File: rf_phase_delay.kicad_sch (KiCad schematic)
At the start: 0 parts

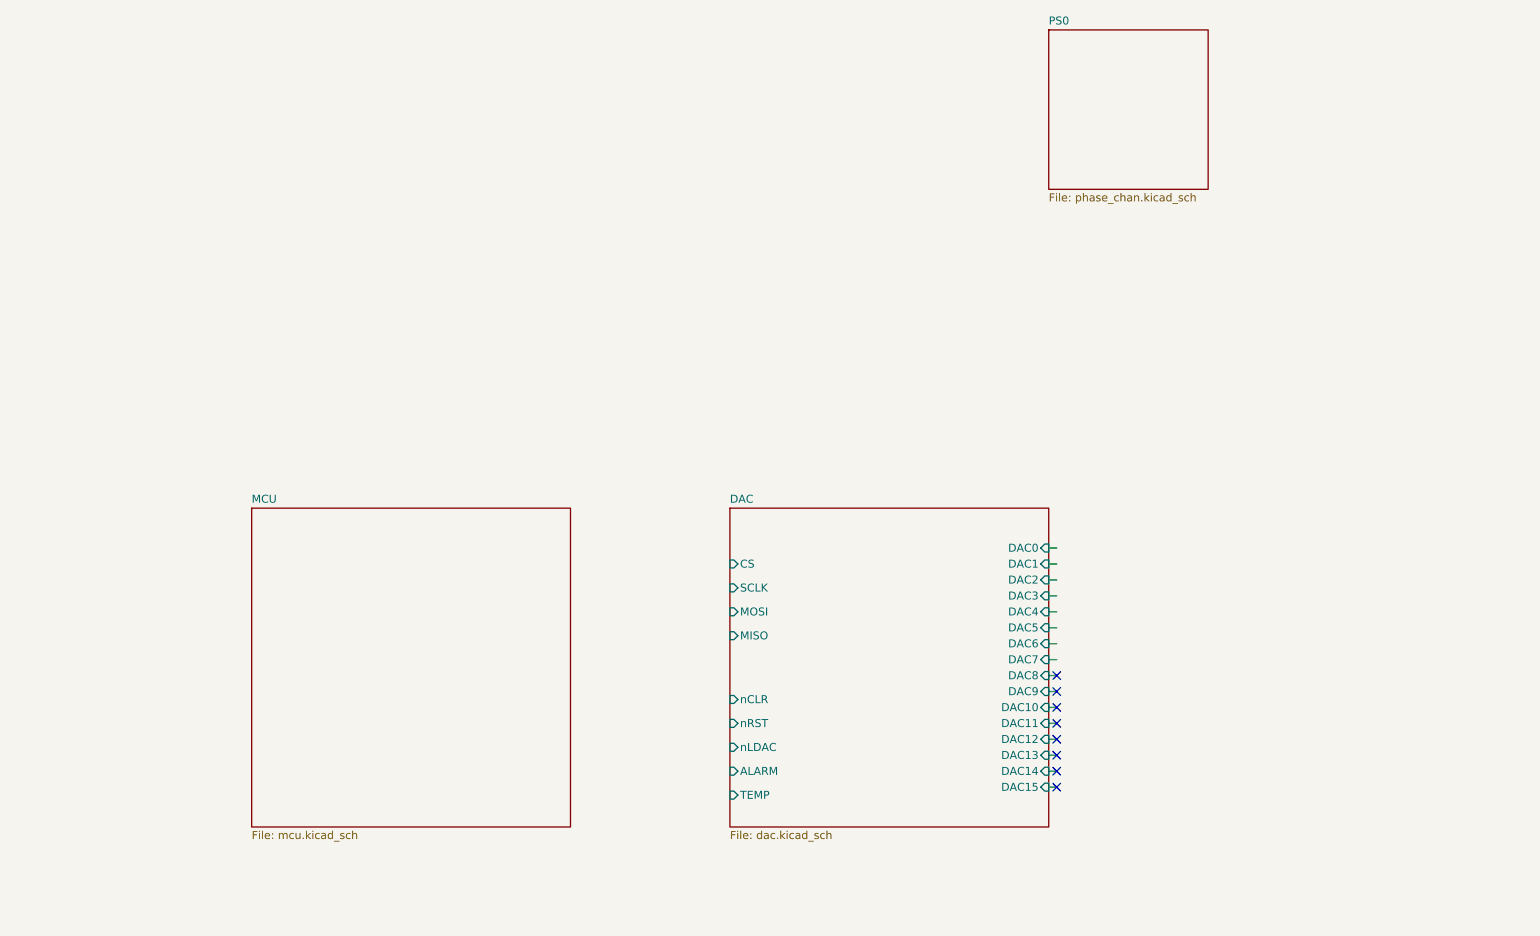
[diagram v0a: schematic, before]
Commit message: Initial MCU IO pinout defined. USB and power sheet created
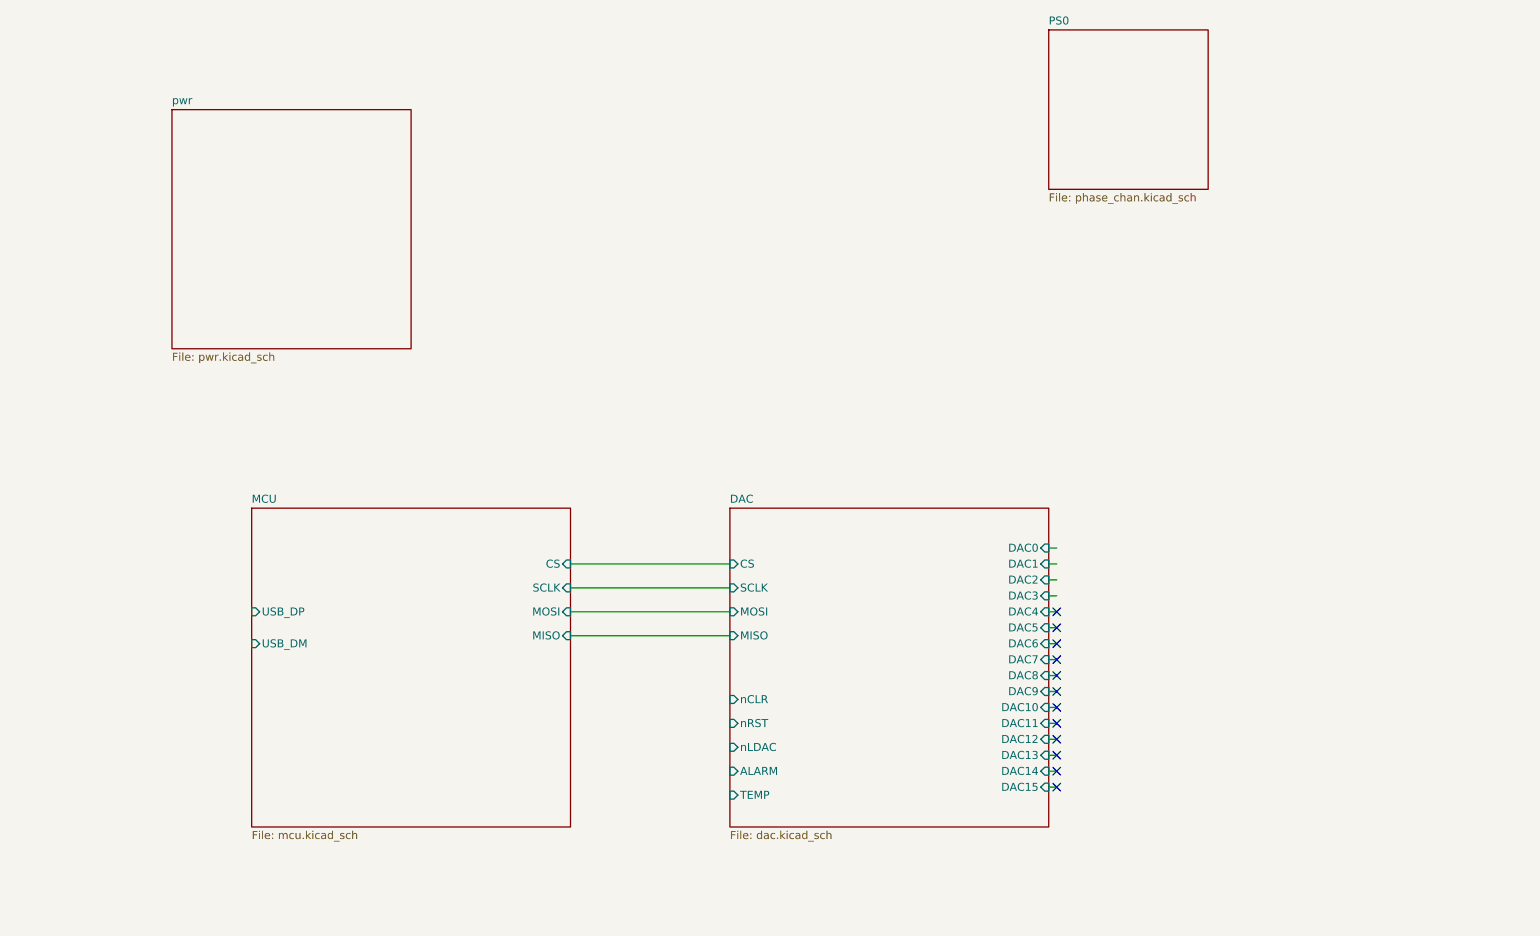
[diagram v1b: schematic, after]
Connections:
- no-connect marks 8 -> 12
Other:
- added sheet pwr (pwr.kicad_sch)
- sheet MCU ports: added CS, MISO, MOSI, SCLK, USB_DM, USB_DP; removed none
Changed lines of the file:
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@@
+	)
+	(no_connect
+		(at 191.77 120.65)
 	)
 	(no_connect
@@
 	)
 	(no_connect
+		(at 191.77 125.73)
+	)
+	(no_connect
+		(at 191.77 118.11)
+	)
+	(no_connect
+		(at 191.77 123.19)
+	)
+	(no_connect
 		(at 191.77 130.81)
 	)
@@
 	(wire
 		(pts
+			(xy 114.3 110.49) (xy 139.7 110.49)
+		)
+		(stroke
+			(width 0)
+			(type default)
+		)
+	)
+	(wire
+		(pts
 			(xy 190.5 113.03) (xy 191.77 113.03)
 		)
@@
 	(wire
 		(pts
+			(xy 114.3 118.11) (xy 139.7 118.11)
+		)
+		(stroke
+			(width 0)
+			(type default)
+		)
+	)
+	(wire
+		(pts
 			(xy 190.5 110.49) (xy 191.77 110.49)
 		)
@@
 	(wire
 		(pts
+			(xy 114.3 121.92) (xy 139.7 121.92)
+		)
+		(stroke
+			(width 0)
+			(type default)
+		)
+	)
+	(wire
+		(pts
 			(xy 190.5 133.35) (xy 191.77 133.35)
 		)
@@
 		(pts
 			(xy 190.5 107.95) (xy 191.77 107.95)
+		)
+		(stroke
+			(width 0)
+			(type default)
+		)
+	)
+	(wire
+		(pts
+			(xy 114.3 114.3) (xy 139.7 114.3)
 		)
 		(stroke
@@
 	)
 	(sheet
+		(at 50.8 38.1)
+		(size 38.1 38.1)
+		(fields_autoplaced yes)
+		(stroke
+			(width 0.1524)
+			(type solid)
+		)
+		(fill
+			(color 255 255 255 1.0000)
+		)
+		(property "Sheetname" "pwr"
+			(at 50.8 37.3884 0)
+			(effects
+				(font
+					(size 1.27 1.27)
+				)
+				(justify left bottom)
+			)
+		)
+		(property "Sheetfile" "pwr.kicad_sch"
+			(at 50.8 76.7846 0)
+			(effects
+				(font
+					(size 1.27 1.27)
+				)
+				(justify left top)
+			)
+		)
+		(instances
+			(project "rf_phase_delay"
+				(path "/ecfae643-93f7-4320-971e-1a2690f71d35"
+					(page "5")
+				)
+			)
+		)
+	)
+	(sheet
 		(at 63.5 101.6)
 		(size 50.8 50.8)
@@
 			)
 		)
+		(pin "SCLK" input
+			(at 114.3 114.3 0)
+			(effects
+				(font
+					(size 1.27 1.27)
+				)
+				(justify right)
+			)
+		)
+		(pin "MISO" input
+			(at 114.3 121.92 0)
+			(effects
+				(font
+					(size 1.27 1.27)
+				)
+				(justify right)
+			)
+		)
+		(pin "MOSI" input
+			(at 114.3 118.11 0)
+			(effects
+				(font
+					(size 1.27 1.27)
+				)
+				(justify right)
+			)
+		)
+		(pin "CS" input
+			(at 114.3 110.49 0)
+			(effects
+				(font
+					(size 1.27 1.27)
+				)
+				(justify right)
+			)
+		)
+		(pin "USB_DM" input
+			(at 63.5 123.19 180)
+			(effects
+				(font
+					(size 1.27 1.27)
+				)
+				(justify left)
+			)
+		)
+		(pin "USB_DP" input
+			(at 63.5 118.11 180)
+			(effects
+				(font
+					(size 1.27 1.27)
+				)
+				(justify left)
+			)
+		)

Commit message: sch_0v1 ready for review
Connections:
- no-connect marks 12 -> 15
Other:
- sheet MCU ports: added PB4, PB5, PB6, PB7, PB8, nRST; removed none
- sheet PS0 ports: added VBIAS; removed none
- sheet pwr ports: added ADC_VCC_ENA, USB_DM, USB_DP, nRST; removed none

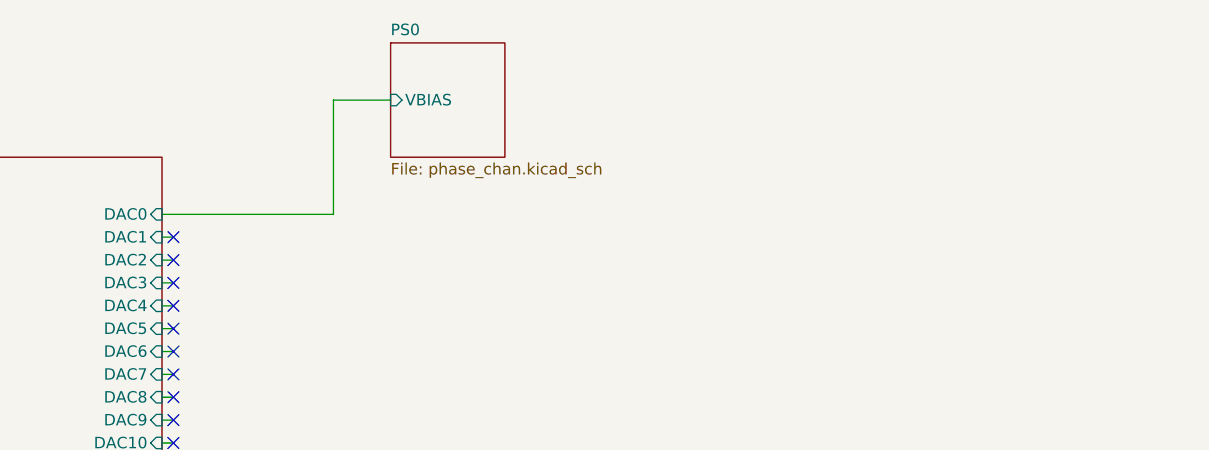
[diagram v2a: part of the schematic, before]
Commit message: created 4 phase controller channel instances
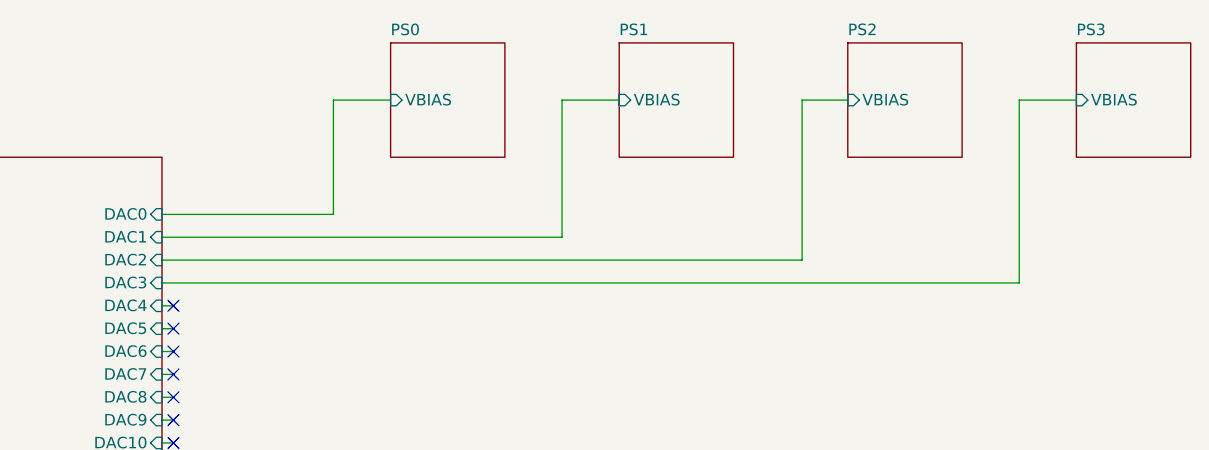
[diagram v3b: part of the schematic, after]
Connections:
- no-connect marks 15 -> 12
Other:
- added sheet PS1 (phase_chan.kicad_sch)
- added sheet PS2 (phase_chan.kicad_sch)
- added sheet PS3 (phase_chan.kicad_sch)
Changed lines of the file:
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@@
-	)
-	(no_connect
-		(at 153.67 46.99)
 	)
 	(no_connect
@@
 	)
 	(no_connect
-		(at 153.67 52.07)
-	)
-	(no_connect
 		(at 153.67 69.85)
 	)
@@
 	)
 	(no_connect
-		(at 153.67 49.53)
-	)
-	(no_connect
 		(at 153.67 54.61)
 	)
@@
 	(wire
 		(pts
+			(xy 247.65 31.75) (xy 254 31.75)
+		)
+		(stroke
+			(width 0)
+			(type default)
+		)
+	)
+	(wire
+		(pts
 			(xy 38.1 127) (xy 25.4 127)
 		)
@@
 	(wire
 		(pts
-			(xy 152.4 49.53) (xy 153.67 49.53)
+			(xy 152.4 49.53) (xy 223.52 49.53)
 		)
 		(stroke
@@
 	(wire
 		(pts
-			(xy 152.4 52.07) (xy 153.67 52.07)
+			(xy 152.4 52.07) (xy 247.65 52.07)
 		)
 		(stroke
@@
 	(wire
 		(pts
-			(xy 152.4 46.99) (xy 153.67 46.99)
+			(xy 152.4 46.99) (xy 196.85 46.99)
 		)
 		(stroke
@@
 	(wire
 		(pts
+			(xy 247.65 52.07) (xy 247.65 31.75)
+		)
+		(stroke
+			(width 0)
+			(type default)
+		)
+	)
+	(wire
+		(pts
 			(xy 152.4 77.47) (xy 153.67 77.47)
 		)
@@
 	(wire
 		(pts
+			(xy 196.85 31.75) (xy 203.2 31.75)
+		)
+		(stroke
+			(width 0)
+			(type default)
+		)
+	)
+	(wire
+		(pts
 			(xy 177.8 31.75) (xy 171.45 31.75)
 		)
@@
 	(wire
 		(pts
+			(xy 196.85 46.99) (xy 196.85 31.75)
+		)
+		(stroke
+			(width 0)
+			(type default)
+		)
+	)
+	(wire
+		(pts
+			(xy 223.52 49.53) (xy 223.52 31.75)
+		)
+		(stroke
+			(width 0)
+			(type default)
+		)
+	)
+	(wire
+		(pts
+			(xy 223.52 31.75) (xy 228.6 31.75)
+		)
+		(stroke
+			(width 0)
+			(type default)
+		)
+	)
+	(wire
+		(pts
 			(xy 25.4 50.8) (xy 38.1 50.8)
 		)
@@
 			(width 0)
 			(type default)
+		)
+	)
+	(sheet
+		(at 203.2 25.4)
+		(size 12.7 12.7)
+		(fields_autoplaced yes)
+		(stroke
+			(width 0.1524)
+			(type solid)
+		)
+		(fill
+			(color 255 255 255 1.0000)
+		)
+		(property "Sheetname" "PS1"
+			(at 203.2 24.6884 0)
+			(effects
+				(font
+					(size 1.27 1.27)
+				)
+				(justify left bottom)
+			)
+		)
+		(property "Sheetfile" "phase_chan.kicad_sch"
+			(at 203.2 38.6846 0)
+			(effects
+				(font
+					(size 1.27 1.27)
+				)
+				(justify left top)
+				(hide yes)
+			)
+		)
+		(pin "VBIAS" input
+			(at 203.2 31.75 180)
+			(effects
+				(font
+					(size 1.27 1.27)
+				)
+				(justify left)
+			)
+		)
+		(instances
+			(project "rf_phase_delay"
+				(path "/ecfae643-93f7-4320-971e-1a2690f71d35"
+					(page "6")
+				)
+			)
 		)
 	)
@@
 				)
 				(justify left top)
+				(hide yes)
 			)
 		)
@@
 	)
 	(sheet
+		(at 228.6 25.4)
+		(size 12.7 12.7)
+		(fields_autoplaced yes)
+		(stroke
+			(width 0.1524)
+			(type solid)
+		)
+		(fill
+			(color 255 255 255 1.0000)
+		)
+		(property "Sheetname" "PS2"
+			(at 228.6 24.6884 0)
+			(effects
+				(font
+					(size 1.27 1.27)
+				)
+				(justify left bottom)
+			)
+		)
+		(property "Sheetfile" "phase_chan.kicad_sch"
+			(at 228.6 38.6846 0)
+			(effects
+				(font
+					(size 1.27 1.27)
+				)
+				(justify left top)
+				(hide yes)
+			)
+		)
+		(pin "VBIAS" input
+			(at 228.6 31.75 180)
+			(effects
+				(font
+					(size 1.27 1.27)
+				)
+				(justify left)
+			)
+		)
+		(instances
+			(project "rf_phase_delay"
+				(path "/ecfae643-93f7-4320-971e-1a2690f71d35"
+					(page "7")
+				)
+			)
+		)
+	)
+	(sheet
 		(at 101.6 38.1)
 		(size 50.8 50.8)
@@
 				)
 			)
+		)
+	)
+	(sheet
+		(at 254 25.4)
+		(size 12.7 12.7)
+		(fields_autoplaced yes)
+		(stroke
+			(width 0.1524)
+			(type solid)
+		)
+		(fill
+			(color 255 255 255 1.0000)
+		)
+		(property "Sheetname" "PS3"
+			(at 254 24.6884 0)
+			(effects
+				(font
+					(size 1.27 1.27)
+				)
+				(justify left bottom)
+			)
+		)
+		(property "Sheetfile" "phase_chan.kicad_sch"
+			(at 254 38.6846 0)
+			(effects
+				(font
+					(size 1.27 1.27)
+				)
+				(justify left top)
+				(hide yes)
+			)
+		)
+		(pin "VBIAS" input
+			(at 254 31.75 180)
+			(effects
+				(font
+					(size 1.27 1.27)
+				)
+				(justify left)
+			)
+		)
+		(instances
+			(project "rf_phase_delay"
+				(path "/ecfae643-93f7-4320-971e-1a2690f71d35"
+					(page "8")
+				)
+			)
